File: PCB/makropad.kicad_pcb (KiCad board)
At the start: 2 copper layers, 82 x 85 mm, 53 parts, among them J1 OLED_DISPLAY, J2 Conn_01x04, J3 Conn_01x04, J4 Conn_01x04, J5 Conn_01x04, SW1 SW_Push_45deg, SW10 SW_Push_45deg, SW11 RotaryEncoder_Switch, SW12 RotaryEncoder_Switch, SW2 SW_Push_45deg, SW3 SW_Push_45deg, SW4 SW_Push_45deg, SW5 SW_Push_45deg, SW6 SW_Push_45deg, SW7 SW_Push_45deg, SW8 SW_Push_45deg, SW9 SW_Push_45deg, U1 PCF8574A, U2 MOUDLE-SEEEDUINO-XIAO

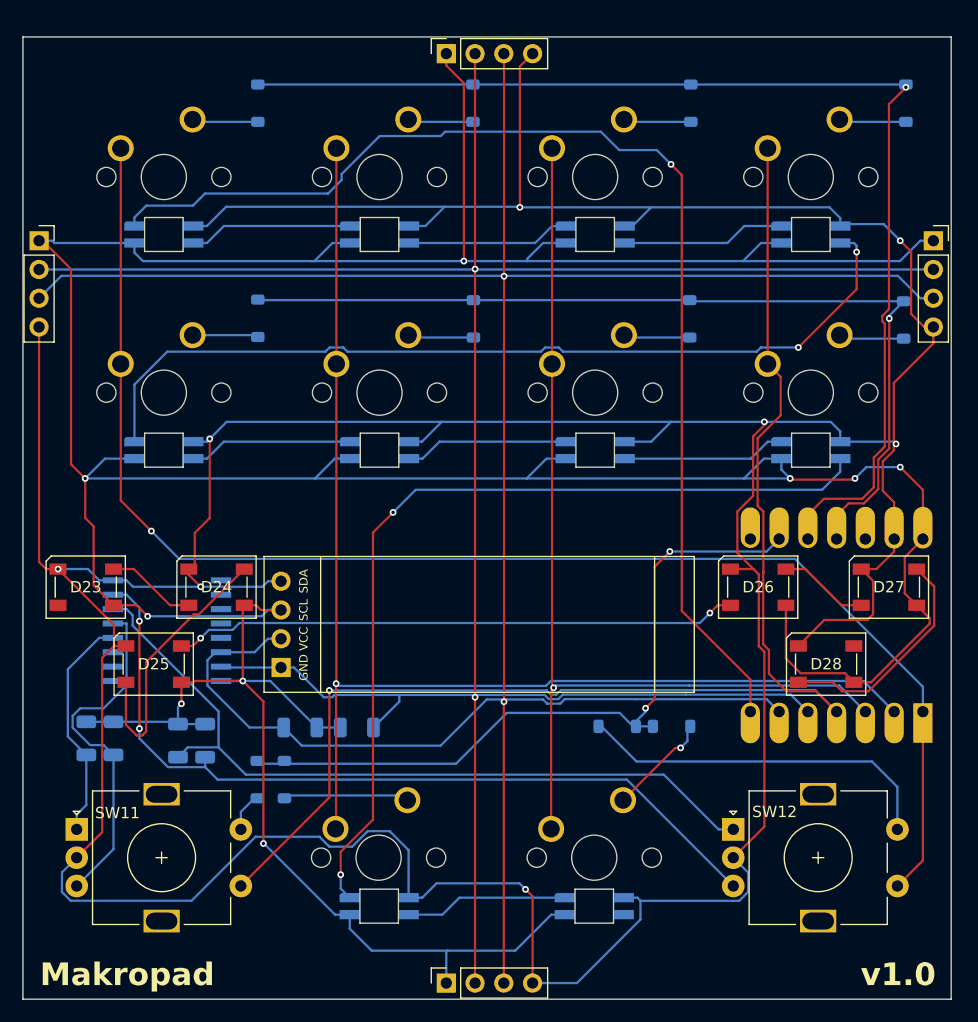
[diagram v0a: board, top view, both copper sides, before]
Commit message: fix: led spacing on bottom switches
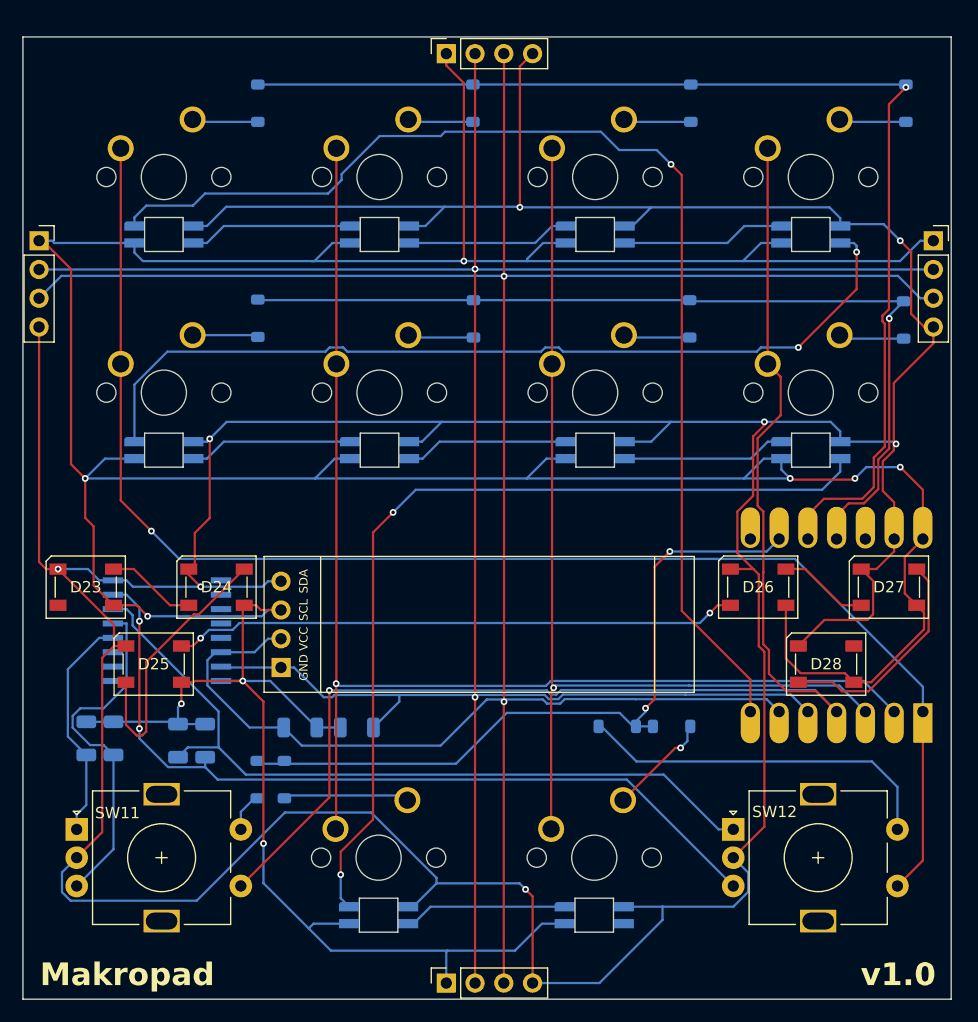
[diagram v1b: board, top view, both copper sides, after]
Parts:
- moved D21 0.80 mm to (142.9, 120.6)
- moved D22 0.80 mm to (162.0, 120.6)
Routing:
- net VCC: track 384.1 -> 388.4 mm
- net GND: track 428.4 -> 430.7 mm
- net Net-(D20-DOUT): track 78.4 -> 79.2 mm

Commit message: feat: add mounting holes and move around some components & silkscreen
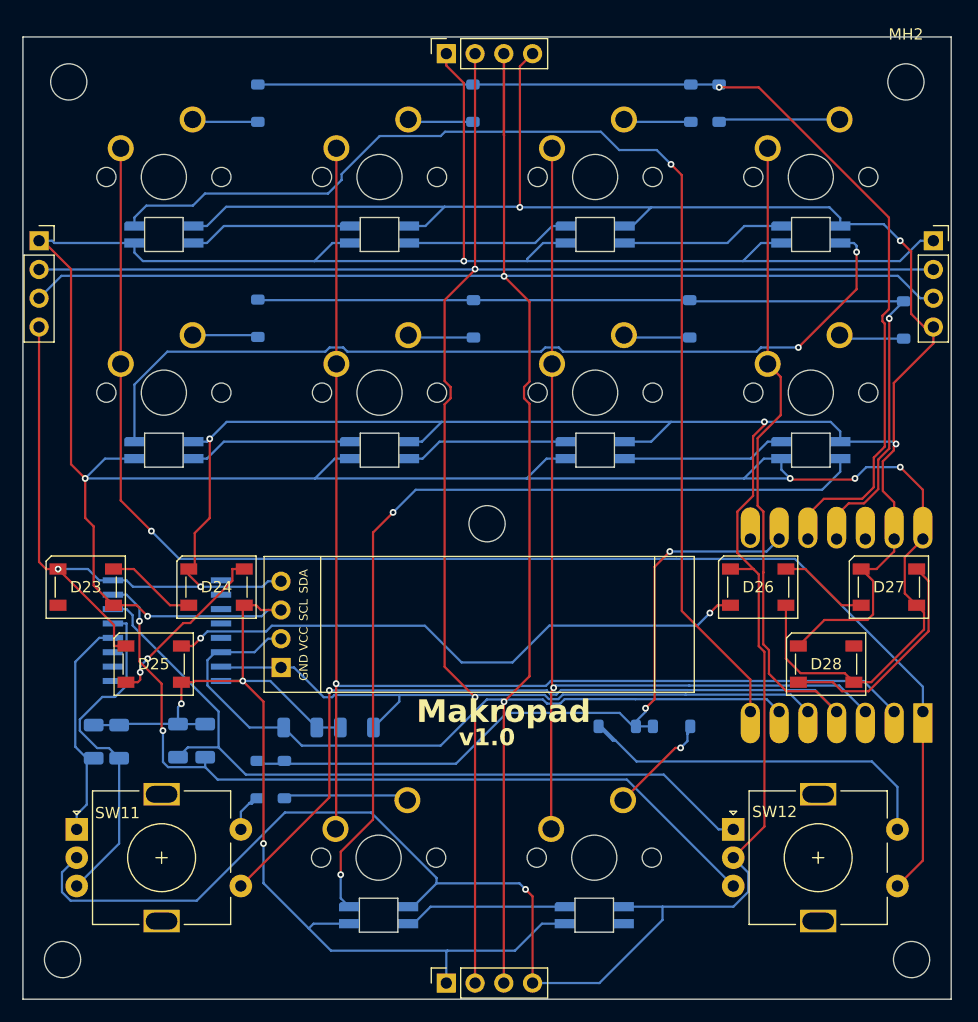
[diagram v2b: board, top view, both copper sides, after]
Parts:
- added MH1: MountingHole_3.2mm_M3, MountingHole:MountingHole_3.2mm_M3, F.Cu at (115.5, 47.0)
- added MH2: MountingHole_3.2mm_M3, MountingHole:MountingHole_3.2mm_M3, F.Cu at (189.5, 47.0)
- added MH4: MountingHole_3.2mm_M3, MountingHole:MountingHole_3.2mm_M3, F.Cu at (152.5, 86.0)
- added MH4: MountingHole_3.2mm_M3, MountingHole:MountingHole_3.2mm_M3, F.Cu at (115.0, 124.5)
- added MH5: MountingHole_3.2mm_M3, MountingHole:MountingHole_3.2mm_M3, F.Cu at (190.0, 124.5)
- moved D4 16.5 mm to (173.0, 48.9)
- moved R6 0.71 mm to (117.8, 105.2)
- moved R5 0.58 mm to (120.0, 105.2)
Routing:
- net GND: track 430.7 -> 410.7 mm
- net I2C_SCL: track 227.6 -> 237.1 mm
- net ROW0: track 102.9 -> 94.3 mm
- net Net-(D24-DOUT): track 24.3 -> 15.9 mm, vias 0 -> 2
- net Net-(D4-A): track 5.95 -> 10.7 mm
- net I2C_SDA: track 219.1 -> 221.8 mm
- net Net-(D25-DOUT): track 50.0 -> 52.7 mm
- net ENC_2_SWA: track 32.1 -> 34.1 mm
- net VCC: track 388.4 -> 387.5 mm
- net ENC_1_SWA: track 3.60 -> 4.52 mm
- net Net-(D11-A): track 9.15 -> 9.91 mm
- net ENC_1_B: track 31.1 -> 30.4 mm

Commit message: feat: switch to gateron low profile
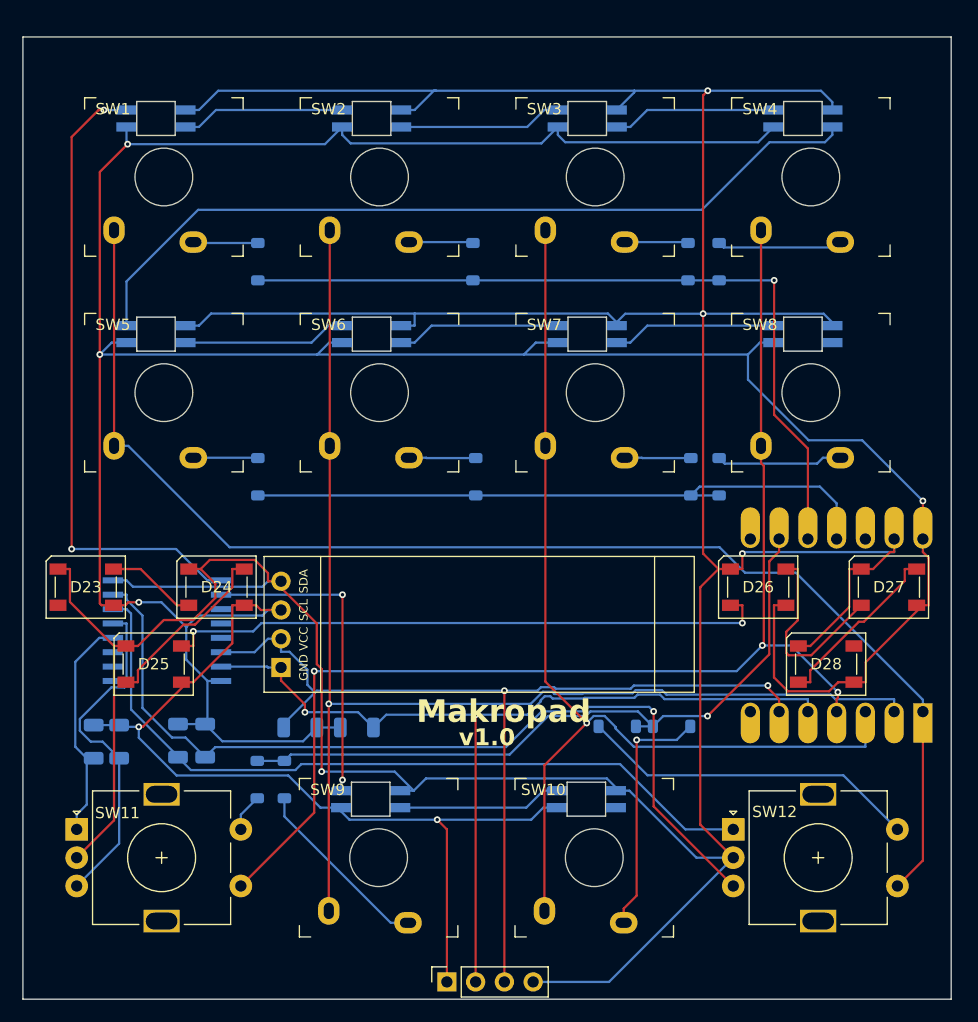
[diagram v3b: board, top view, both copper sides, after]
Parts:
- removed J3, J4, J5: Conn_01x04, Components:4pin
- removed MH1, MH2, MH4 (x2), MH5: MountingHole_3.2mm_M3, MountingHole:MountingHole_3.2mm_M3
- SW1, SW10, SW2, SW3, SW4, SW5, SW6, SW7, SW8, SW9: footprint Components:MX-Solderable-1U -> Components:Gateron Low Profile Switch 2.0
- moved J2 74.7 mm to (148.9, 126.5), turned to 90 degrees
- moved D8 21.4 mm to (173.0, 81.8), turned to 90 degrees
- moved D3 14.0 mm to (170.2, 62.9), turned to 90 degrees
- moved D1 14.0 mm to (132.2, 62.9), turned to 90 degrees
- moved D2 14.0 mm to (151.2, 62.9), turned to 90 degrees
- moved D4 14.0 mm to (173.0, 62.9), turned to 90 degrees
- moved D5 14.0 mm to (132.2, 81.8), turned to 90 degrees
- moved D6 14.0 mm to (151.5, 81.8), turned to 90 degrees
- moved D7 14.0 mm to (170.5, 81.8), turned to 90 degrees
- moved D13 10.3 mm to (123.2, 50.2)
- moved D15 10.3 mm to (161.3, 50.2)
- moved D17 10.3 mm to (123.2, 69.2)
- moved D19 10.3 mm to (161.3, 69.2)
- moved D14 10.3 mm to (142.3, 50.2)
- moved D16 10.3 mm to (180.4, 50.2)
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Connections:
- D20 pad 4: Net-(D20-DOUT) -> unconnected-(D20-DOUT-Pad4)
- D21 pad 2: Net-(D20-DOUT) -> RGB2
- U1 pad 10: unconnected-(U1-P5-Pad10) -> RGB2
- U1 pad 9: unconnected-(U1-P4-Pad9) -> RGB
- U2 pad 7: RGB -> unconnected-(U2-PB08_A6_D6_TX-Pad7)
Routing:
- net I2C_SCL: track 237.1 -> 85.4 mm
- net I2C_SDA: track 221.8 -> 81.7 mm
- net Net-(D20-DOUT): track 79.2 -> 0.00 mm, vias 2 -> 0
- net RGB: track 104.0 -> 56.6 mm, vias 1 -> 2
- net VCC: track 387.5 -> 354.4 mm, vias 9 -> 6
- net GND: track 410.7 -> 380.8 mm, vias 8 -> 4
- net RGB2: track 0.00 -> 28.1 mm, vias 0 -> 2
- net ROW0: track 94.3 -> 69.7 mm
- net ROW1: track 81.4 -> 57.7 mm, vias 1 -> 0
- net COL3: track 122.0 -> 109.2 mm, vias 1 -> 3
- net Net-(D11-A): track 9.91 -> 21.9 mm
- net COL0: track 127.3 -> 117.2 mm, vias 1 -> 0
- net Net-(D26-DOUT): track 7.98 -> 17.4 mm
- net Net-(D16-DOUT): track 78.3 -> 72.3 mm, vias 2 -> 0
- net ENC_2_B: track 73.1 -> 79.1 mm, vias 2 -> 1
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
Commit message: feat: add mounting holes for new design
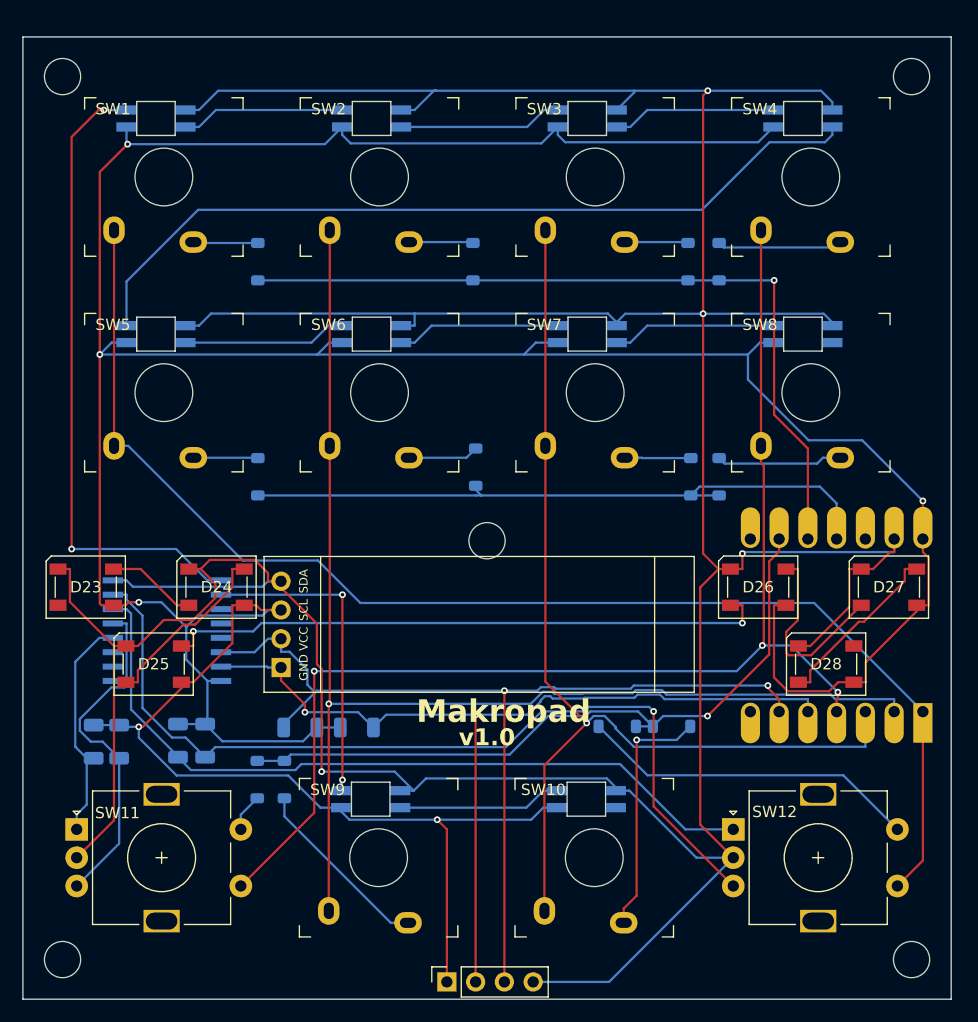
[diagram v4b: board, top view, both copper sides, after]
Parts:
- added MH1: MountingHole_3.2mm_M3, MountingHole:MountingHole_3.2mm_M3, F.Cu at (115.0, 46.5)
- added MH2: MountingHole_3.2mm_M3, MountingHole:MountingHole_3.2mm_M3, F.Cu at (190.0, 46.5)
- added MH3: MountingHole_3.2mm_M3, MountingHole:MountingHole_3.2mm_M3, F.Cu at (115.0, 124.5)
- added MH4: MountingHole_3.2mm_M3, MountingHole:MountingHole_3.2mm_M3, F.Cu at (152.5, 87.5)
- added MH4: MountingHole_3.2mm_M3, MountingHole:MountingHole_3.2mm_M3, F.Cu at (190.0, 124.5)
- moved D6 0.85 mm to (151.5, 81.0)
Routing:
- net ROW1: track 57.7 -> 58.8 mm
- net COL0: track 117.2 -> 116.6 mm
